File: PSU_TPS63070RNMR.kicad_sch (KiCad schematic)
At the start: 8 parts, among them U10 TPS63070

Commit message: bom updates
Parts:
- removed C25: C386081, robot-cortex:C_0603_1608Metric, symbol foc-pcb:Capacitor_small
- removed C29, C30: C2998534, robot-cortex:C_0603_1608Metric, symbol foc-pcb:Capacitor_small
- added C22, C32, C33: 10uF, robot-cortex:C_0603_1608Metric, symbol foc-pcb:Capacitor_small
- C27: value C2998534 -> 10uF; Dielectric (none) -> X5R; Package Size (none) -> 0603; Voltage Rating (none) -> 10V
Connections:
- net FB_VOUT: now also C32.1, C33.1
- net GND: now also C22.2, C32.2, C33.2
- net VIN: now also C22.1
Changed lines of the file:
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@@
 (kicad_sch (version 20230121) (generator eeschema)
   (paper "A4")
+  (junction (at 177.8 83.185) (diameter 0) (color 0 0 0 0)
+  )
+  (junction (at 177.8 78.105) (diameter 0) (color 0 0 0 0)
+  )
+  (junction (at 135.89 98.425) (diameter 0) (color 0 0 0 0)
+  )
   (junction (at 109.22 78.105) (diameter 0) (color 0 0 0 0)
   )
-  (junction (at 135.89 98.425) (diameter 0) (color 0 0 0 0)
-  )
   (junction (at 135.89 95.885) (diameter 0) (color 0 0 0 0)
   )
   (junction (at 164.465 78.105) (diameter 0) (color 0 0 0 0)
   )
-  (junction (at 177.8 78.105) (diameter 0) (color 0 0 0 0)
-  )
   (junction (at 112.395 78.105) (diameter 0) (color 0 0 0 0)
   )
   (junction (at 183.515 78.105) (diameter 0) (color 0 0 0 0)
   )
-  (junction (at 177.8 83.185) (diameter 0) (color 0 0 0 0)
-  )
   (junction (at 144.145 78.105) (diameter 0) (color 0 0 0 0)
   )
@@
     (stroke (width 0) (type default))
   )
+  (wire (pts (xy 137.795 64.77) (xy 132.715 64.77))
+    (stroke (width 0) (type default))
+  )
+  (wire (pts (xy 135.89 75.565) (xy 137.795 75.565))
+    (stroke (width 0) (type default))
+  )
+  (wire (pts (xy 109.22 76.835) (xy 109.22 78.105))
+    (stroke (width 0) (type default))
+  )
+  (wire (pts (xy 135.89 95.885) (xy 135.89 98.425))
+    (stroke (width 0) (type default))
+  )
+  (wire (pts (xy 109.22 78.105) (xy 112.395 78.105))
+    (stroke (width 0) (type default))
+  )
   (wire (pts (xy 177.8 78.105) (xy 183.515 78.105))
-    (stroke (width 0) (type default))
-  )
-  (wire (pts (xy 137.795 64.77) (xy 132.715 64.77))
-    (stroke (width 0) (type default))
-  )
-  (wire (pts (xy 135.89 75.565) (xy 137.795 75.565))
-    (stroke (width 0) (type default))
-  )
-  (wire (pts (xy 109.22 76.835) (xy 109.22 78.105))
-    (stroke (width 0) (type default))
-  )
-  (wire (pts (xy 135.89 95.885) (xy 135.89 98.425))
-    (stroke (width 0) (type default))
-  )
-  (wire (pts (xy 109.22 78.105) (xy 112.395 78.105))
     (stroke (width 0) (type default))
   )
@@
     )
   )
+  (symbol (lib_id "foc-pcb:Capacitor_small") (at 109.22 80.645 0) (mirror y) (unit 1)
+    (in_bom yes) (on_board yes) (dnp no)
+    (property "Reference" "C22" (at 106.68 80.01 0)
+      (effects (font (size 1.27 1.27)) (justify left))
+    )
+    (property "Value" "10uF " (at 106.68 82.55 0)
+      (effects (font (size 1.27 1.27)) (justify left))
+    )
+    (property "Footprint" "robot-cortex:C_0603_1608Metric" (at 108.2548 84.455 0)
+      (effects (font (size 1.27 1.27)) hide)
+    )
+    (property "Datasheet" "~" (at 109.22 80.645 0)
+      (effects (font (size 1.27 1.27)) hide)
+    )
+    (property "Voltage Rating" "10V " (at 109.22 80.645 0)
+      (effects (font (size 1.27 1.27)) hide)
+    )
+    (property "Dielectric" "X5R" (at 109.22 80.645 0)
+      (effects (font (size 1.27 1.27)) hide)
+    )
+    (property "Package Size" " 0603" (at 109.22 80.645 0)
+      (effects (font (size 1.27 1.27)) hide)
+    )
+    (pin "1")
+    (pin "2")
+    (instances
+      (project "robot-cortex"
+        (path "/19e4cb9f-d0a4-4ce0-8aa4-5fe95563dc37/957a9604-35b3-4788-b08c-3ca047cc62dc"
+          (reference "C22") (unit 1)
+        )
+        (path "/19e4cb9f-d0a4-4ce0-8aa4-5fe95563dc37/66225d13-410c-4182-8e7e-33506c71e2e4"
+          (reference "C25") (unit 1)
+        )
+      )
+    )
+  )
   (symbol (lib_id "foc-pcb:Capacitor_small") (at 183.515 80.645 0) (unit 1)
-    (in_bom yes) (on_board yes) (dnp no)
-    (property "Reference" "C30" (at 184.785 79.375 0)
-      (effects (font (size 1.27 1.27)) (justify left))
-    )
-    (property "Value" "C2998534" (at 184.785 82.55 0)
+    (in_bom yes) (on_board yes) (dnp no) (fields_autoplaced)
+    (property "Reference" "C33" (at 186.055 80.01 0)
+      (effects (font (size 1.27 1.27)) (justify left))
+    )
+    (property "Value" "10uF " (at 186.055 82.55 0)
       (effects (font (size 1.27 1.27)) (justify left))
     )
@@
       (effects (font (size 1.27 1.27)) hide)
     )
-    (pin "1")
-    (pin "2")
-    (instances
-      (project "robot-cortex"
-        (path "/19e4cb9f-d0a4-4ce0-8aa4-5fe95563dc37/66225d13-410c-4182-8e7e-33506c71e2e4"
-          (reference "C30") (unit 1)
-        )
+    (property "Voltage Rating" "10V " (at 183.515 80.645 0)
+      (effects (font (size 1.27 1.27)) hide)
+    )
+    (property "Dielectric" "X5R" (at 183.515 80.645 0)
+      (effects (font (size 1.27 1.27)) hide)
+    )
+    (property "Package Size" " 0603" (at 183.515 80.645 0)
+      (effects (font (size 1.27 1.27)) hide)
+    )
+    (pin "1")
+    (pin "2")
+    (instances
+      (project "robot-cortex"
         (path "/19e4cb9f-d0a4-4ce0-8aa4-5fe95563dc37/957a9604-35b3-4788-b08c-3ca047cc62dc"
           (reference "C33") (unit 1)
         )
-      )
-      (project "foc-pcb"
-        (path "/2b52ab19-a93e-4439-8602-a1380e4825c0"
-          (reference "C23") (unit 1)
-        )
-        (path "/2b52ab19-a93e-4439-8602-a1380e4825c0/1dc3938b-02e0-4f20-a5f4-e30fb517d809"
-          (reference "C25") (unit 1)
-        )
-      )
-    )
-  )
-  (symbol (lib_id "foc-pcb:Capacitor_small") (at 109.22 80.645 0) (mirror y) (unit 1)
-    (in_bom yes) (on_board yes) (dnp no) (fields_autoplaced)
-    (property "Reference" "C25" (at 106.68 80.01 0)
-      (effects (font (size 1.27 1.27)) (justify left))
-    )
-    (property "Value" "C386081" (at 106.68 82.55 0)
-      (effects (font (size 1.27 1.27)) (justify left))
-    )
-    (property "Footprint" "robot-cortex:C_0603_1608Metric" (at 108.2548 84.455 0)
-      (effects (font (size 1.27 1.27)) hide)
-    )
-    (property "Datasheet" "~" (at 109.22 80.645 0)
-      (effects (font (size 1.27 1.27)) hide)
-    )
-    (pin "1")
-    (pin "2")
-    (instances
-      (project "robot-cortex"
-        (path "/19e4cb9f-d0a4-4ce0-8aa4-5fe95563dc37/66225d13-410c-4182-8e7e-33506c71e2e4"
-          (reference "C25") (unit 1)
-        )
-        (path "/19e4cb9f-d0a4-4ce0-8aa4-5fe95563dc37/957a9604-35b3-4788-b08c-3ca047cc62dc"
-          (reference "C22") (unit 1)
-        )
-      )
-      (project "foc-pcb"
-        (path "/2b52ab19-a93e-4439-8602-a1380e4825c0"
-          (reference "C24") (unit 1)
-        )
-        (path "/2b52ab19-a93e-4439-8602-a1380e4825c0/1dc3938b-02e0-4f20-a5f4-e30fb517d809"
-          (reference "C20") (unit 1)
-        )
-      )
-    )
-  )
-  (symbol (lib_id "foc-pcb:Capacitor_small") (at 177.8 80.645 0) (unit 1)
-    (in_bom yes) (on_board yes) (dnp no)
-    (property "Reference" "C29" (at 178.435 79.375 0)
-      (effects (font (size 1.27 1.27)) (justify left))
-    )
-    (property "Value" "C2998534" (at 177.8 76.835 90)
-      (effects (font (size 1.27 1.27)) (justify left))
-    )
-    (property "Footprint" "robot-cortex:C_0603_1608Metric" (at 178.7652 84.455 0)
-      (effects (font (size 1.27 1.27)) hide)
-    )
-    (property "Datasheet" "~" (at 177.8 80.645 0)
-      (effects (font (size 1.27 1.27)) hide)
-    )
-    (pin "1")
-    (pin "2")
-    (instances
-      (project "robot-cortex"
         (path "/19e4cb9f-d0a4-4ce0-8aa4-5fe95563dc37/66225d13-410c-4182-8e7e-33506c71e2e4"
           (reference "C29") (unit 1)
-        )
-        (path "/19e4cb9f-d0a4-4ce0-8aa4-5fe95563dc37/957a9604-35b3-4788-b08c-3ca047cc62dc"
-          (reference "C32") (unit 1)
-        )
-      )
-      (project "foc-pcb"
-        (path "/2b52ab19-a93e-4439-8602-a1380e4825c0"
-          (reference "C22") (unit 1)
-        )
-        (path "/2b52ab19-a93e-4439-8602-a1380e4825c0/1dc3938b-02e0-4f20-a5f4-e30fb517d809"
-          (reference "C24") (unit 1)
         )
       )
@@
       (effects (font (size 1.27 1.27)) hide)
     )
-    (property "Datasheet" "" (at 123.19 88.265 0)
+    (property "Datasheet" "https://www.ti.com/lit/ds/symlink/tps63070.pdf" (at 123.19 88.265 0)
       (effects (font (size 1.27 1.27)) hide)
     )
@@
       (effects (font (size 1.27 1.27)) (justify left))
     )
-    (property "Value" "C2998534" (at 146.685 82.55 0)
+    (property "Value" "10uF " (at 146.685 82.55 0)
       (effects (font (size 1.27 1.27)) (justify left))
     )
@@
       (effects (font (size 1.27 1.27)) hide)
     )
+    (property "Voltage Rating" "10V " (at 144.145 80.645 0)
+      (effects (font (size 1.27 1.27)) hide)
+    )
+    (property "Dielectric" "X5R" (at 144.145 80.645 0)
+      (effects (font (size 1.27 1.27)) hide)
+    )
+    (property "Package Size" " 0603" (at 144.145 80.645 0)
+      (effects (font (size 1.27 1.27)) hide)
+    )
     (pin "1")
     (pin "2")
@@
         )
       )
+    )
+  )
+  (symbol (lib_id "foc-pcb:Capacitor_small") (at 177.8 80.645 0) (mirror y) (unit 1)
+    (in_bom yes) (on_board yes) (dnp no)
+    (property "Reference" "C32" (at 175.895 80.01 0)
+      (effects (font (size 1.27 1.27)) (justify left))
+    )
+    (property "Value" "10uF " (at 177.165 82.55 0)
+      (effects (font (size 1.27 1.27)) (justify left))
+    )
+    (property "Footprint" "robot-cortex:C_0603_1608Metric" (at 176.8348 84.455 0)
+      (effects (font (size 1.27 1.27)) hide)
+    )
+    (property "Datasheet" "~" (at 177.8 80.645 0)
+      (effects (font (size 1.27 1.27)) hide)
+    )
+    (property "Voltage Rating" "10V " (at 177.8 80.645 0)
+      (effects (font (size 1.27 1.27)) hide)
+    )
+    (property "Dielectric" "X5R" (at 177.8 80.645 0)
+      (effects (font (size 1.27 1.27)) hide)
+    )
+    (property "Package Size" " 0603" (at 177.8 80.645 0)
+      (effects (font (size 1.27 1.27)) hide)
+    )
+    (pin "1")
+    (pin "2")
+    (instances
+      (project "robot-cortex"
+        (path "/19e4cb9f-d0a4-4ce0-8aa4-5fe95563dc37/957a9604-35b3-4788-b08c-3ca047cc62dc"
+          (reference "C32") (unit 1)
+        )
+        (path "/19e4cb9f-d0a4-4ce0-8aa4-5fe95563dc37/66225d13-410c-4182-8e7e-33506c71e2e4"
+          (reference "C30") (unit 1)
+        )
+      )

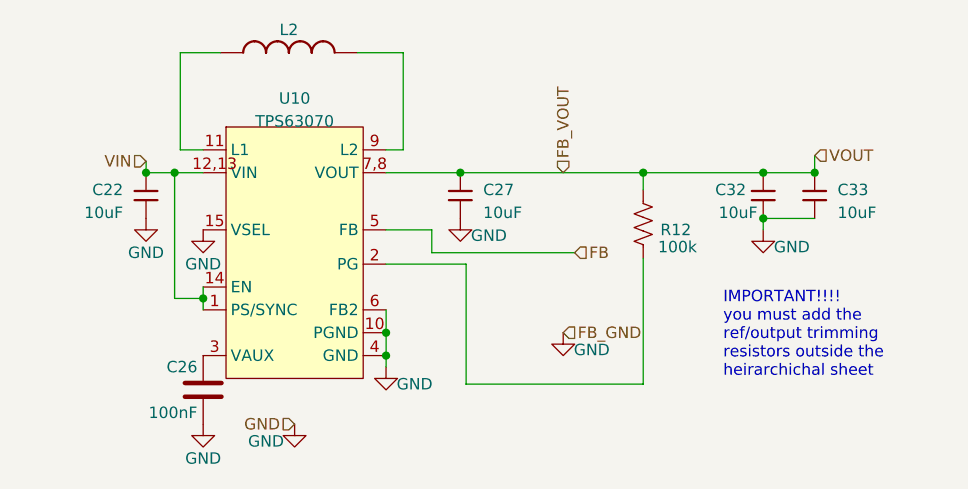
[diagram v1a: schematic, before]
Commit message: bom cleanup - caps not hardcoded lcsc part, led replaced
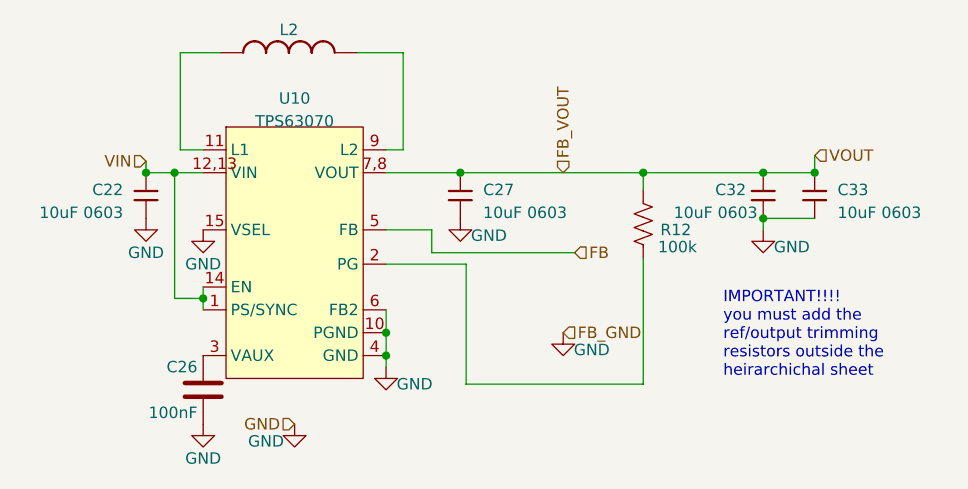
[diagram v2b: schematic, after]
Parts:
- C22, C27, C32, C33: value 10uF -> 10uF 0603
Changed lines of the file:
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@@
       (effects (font (size 1.27 1.27)) (justify left))
     )
-    (property "Value" "10uF " (at 106.68 82.55 0)
+    (property "Value" "10uF 0603 " (at 106.68 82.55 0)
       (effects (font (size 1.27 1.27)) (justify left))
     )
@@
       (effects (font (size 1.27 1.27)) (justify left))
     )
-    (property "Value" "10uF " (at 186.055 82.55 0)
+    (property "Value" "10uF 0603 " (at 186.055 82.55 0)
       (effects (font (size 1.27 1.27)) (justify left))
     )
@@
       (effects (font (size 1.27 1.27)) (justify left))
     )
-    (property "Value" "10uF " (at 146.685 82.55 0)
+    (property "Value" "10uF 0603 " (at 146.685 82.55 0)
       (effects (font (size 1.27 1.27)) (justify left))
     )
@@
       (effects (font (size 1.27 1.27)) (justify left))
     )
-    (property "Value" "10uF " (at 177.165 82.55 0)
-      (effects (font (size 1.27 1.27)) (justify left))
-    )
+    (property "Value" "10uF 0603 " (at 177.165 82.55 0)
+      (effects (font (size 1.27 1.27)) (justify left))
+    )

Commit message: final bom cleanup
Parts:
- L2: value 1277AS-H-1R0M=P2 -> 1uH; DCR (none) -> 45mOhm; MPN ETQ-P3M3R3KVP -> 1277AS-H-1R0M=P2
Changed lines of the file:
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@@
       (effects (font (size 1.27 1.27)))
     )
-    (property "Value" "1277AS-H-1R0M=P2" (at 120.015 62.23 0)
+    (property "Value" "1uH" (at 120.015 62.23 0)
       (effects (font (size 1.27 1.27)) hide)
     )
@@
       (effects (font (size 1.27 1.27)) hide)
     )
-    (property "Datasheet" "" (at 125.095 64.77 0)
+    (property "Datasheet" "https://www.murata.com/~/media/webrenewal/products/inductor/chip/tokoproducts/wirewoundmetalalloychiptype/m_dfe322512c.ashx" (at 125.095 64.77 0)
       (effects (font (size 1.27 1.27)) hide)
     )
-    (property "MPN" "ETQ-P3M3R3KVP" (at 125.095 57.15 0)
+    (property "MPN" "1277AS-H-1R0M=P2" (at 125.095 64.77 0)
       (effects (font (size 1.27 1.27)) hide)
     )
+    (property "DCR" "45mOhm" (at 125.095 64.77 0)
+      (effects (font (size 1.27 1.27)) hide)
+    )
